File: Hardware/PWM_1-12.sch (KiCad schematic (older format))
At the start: 0 parts

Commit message: Renamed project
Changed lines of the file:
@@
 encoding utf-8
 Sheet 2 14
-Title ""
-Date ""
+Title "PWM 1-12"
+Date "2017-05-13"
 Rev ""
-Comp ""
-Comment1 ""
+Comp "WARG"
+Comment1 "Author: Stephen Cholvat"
 Comment2 ""
 Comment3 ""
@@
 	2700 950  2450 950
 Wire Wire Line
-	2450 550  2450 650
+	2450 650  2450 650
 Wire Wire Line
 	2450 650  2450 950
@@
 Wire Wire Line
 	7200 1750 8250 1750
-Text HLabel 1100 850  0    60   Input ~ 0
+Text HLabel 1100 950  0    60   Input ~ 0
 OC
-Text HLabel 1100 700  0    60   Input ~ 0
+Text HLabel 1100 800  0    60   Input ~ 0
 PWM
-Text HLabel 1100 1000 0    60   Input ~ 0
+Text HLabel 1100 1100 0    60   Input ~ 0
 SEL
-Text HLabel 1100 550  0    60   Input ~ 0
+Text HLabel 1100 650  0    60   Input ~ 0
 PWM_5V
 Wire Wire Line
-	2450 550  1100 550
+	2450 650  1100 650
 Connection ~ 2450 650
 Wire Bus Line
-	1100 700  1400 700
-Wire Bus Line
-	1100 850  1400 850
-Wire Bus Line
-	1100 1000 1400 1000
-Text Label 1200 700  0    60   ~ 0
+	1100 800  1400 800
+Wire Bus Line
+	1100 950  1400 950
+Wire Bus Line
+	1100 1100 1400 1100
+Text Label 1200 800  0    60   ~ 0
 PWM
-Text Label 1250 850  0    60   ~ 0
+Text Label 1250 950  0    60   ~ 0
 OC
-Text Label 1250 1000 0    60   ~ 0
+Text Label 1250 1100 0    60   ~ 0
 SEL
 $EndSCHEMATC

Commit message: ALL THE POWER
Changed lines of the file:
@@
 LIBS:valves
 LIBS:WARG
+LIBS:ZeroPilot-cache
 EELAYER 25 0
 EELAYER END
 $Descr A4 11693 8268
 encoding utf-8
-Sheet 2 14
+Sheet 2 15
 Title "PWM 1-12"
 Date "2017-05-13"
@@
 F4 "PWM" I L 2700 1250 60
 F5 "OC" I L 2700 1500 60
+F6 "SW_5V" I L 2700 1100 60
 $EndSheet
 $Sheet
@@
 F4 "PWM" I L 2700 2700 60
 F5 "OC" I L 2700 2950 60
+F6 "SW_5V" I L 2700 2550 60
 $EndSheet
 $Sheet
@@
 F4 "PWM" I L 2700 4200 60
 F5 "OC" I L 2700 4450 60
+F6 "SW_5V" I L 2700 4050 60
 $EndSheet
 $Sheet
@@
 F4 "PWM" I L 2700 5650 60
 F5 "OC" I L 2700 5900 60
+F6 "SW_5V" I L 2700 5500 60
 $EndSheet
 $Sheet
@@
 F4 "PWM" I L 5400 1250 60
 F5 "OC" I L 5400 1500 60
+F6 "SW_5V" I L 5400 1100 60
 $EndSheet
 $Sheet
@@
 F4 "PWM" I L 5400 2700 60
 F5 "OC" I L 5400 2950 60
+F6 "SW_5V" I L 5400 2550 60
 $EndSheet
 $Sheet
@@
 F4 "PWM" I L 5400 4200 60
 F5 "OC" I L 5400 4450 60
+F6 "SW_5V" I L 5400 4050 60
 $EndSheet
 $Sheet
@@
 F4 "PWM" I L 5400 5650 60
 F5 "OC" I L 5400 5900 60
+F6 "SW_5V" I L 5400 5500 60
 $EndSheet
 $Sheet
@@
 F4 "PWM" I L 8250 1250 60
 F5 "OC" I L 8250 1500 60
+F6 "SW_5V" I L 8250 1100 60
 $EndSheet
 $Sheet
@@
 F4 "PWM" I L 8250 2700 60
 F5 "OC" I L 8250 2950 60
+F6 "SW_5V" I L 8250 2550 60
 $EndSheet
 $Sheet
@@
 F4 "PWM" I L 8250 4200 60
 F5 "OC" I L 8250 4450 60
+F6 "SW_5V" I L 8250 4050 60
 $EndSheet
 $Sheet
@@
 F4 "PWM" I L 8250 5650 60
 F5 "OC" I L 8250 5900 60
+F6 "SW_5V" I L 8250 5500 60
 $EndSheet
 Entry Wire Line
@@
 SEL12
 Wire Wire Line
-	2700 950  2450 950
-Wire Wire Line
-	2450 650  2450 650
-Wire Wire Line
-	2450 650  2450 950
-Wire Wire Line
-	2450 950  2450 2400
-Wire Wire Line
-	2450 2400 2450 3900
-Wire Wire Line
-	2450 3900 2450 5350
-Wire Wire Line
-	2450 5350 2700 5350
-Wire Wire Line
-	5400 950  5400 2400
-Wire Wire Line
-	5400 2400 5400 3900
-Wire Wire Line
-	5400 3900 5400 5350
-Wire Wire Line
-	5400 950  5100 950
-Wire Wire Line
-	5100 650  5100 950
-Wire Wire Line
-	5100 950  5100 2400
-Wire Wire Line
-	5100 2400 5100 3900
-Wire Wire Line
-	5100 3900 5100 5350
-Wire Wire Line
-	5100 5350 5400 5350
-Wire Wire Line
-	5400 3900 5100 3900
-Connection ~ 5100 3900
-Connection ~ 5400 3900
-Wire Wire Line
-	5400 2400 5100 2400
-Connection ~ 5100 2400
-Connection ~ 5400 2400
-Wire Wire Line
-	8250 950  7950 950
-Wire Wire Line
-	7950 650  7950 950
-Wire Wire Line
-	7950 950  7950 2400
-Wire Wire Line
-	7950 2400 7950 3900
-Wire Wire Line
-	7950 3900 7950 5350
-Wire Wire Line
-	7950 5350 8250 5350
-Wire Wire Line
-	8250 3900 7950 3900
-Connection ~ 7950 3900
-Wire Wire Line
-	8250 2400 7950 2400
-Connection ~ 7950 2400
-Wire Wire Line
-	2450 650  5100 650
-Wire Wire Line
-	5100 650  7950 650
-Connection ~ 2450 950
-Connection ~ 7950 950
-Connection ~ 5100 650
-Connection ~ 5100 950
+	2700 950  2350 950
+Wire Wire Line
+	1100 650  1650 650
+Wire Wire Line
+	2350 5350 2700 5350
+Wire Wire Line
+	5400 950  5000 950
+Wire Wire Line
+	5000 5350 5400 5350
+Wire Wire Line
+	5400 3900 4950 3900
+Wire Wire Line
+	5400 2400 5000 2400
+Wire Wire Line
+	8250 950  7850 950
+Wire Wire Line
+	7850 5350 8250 5350
+Wire Wire Line
+	8250 3900 7800 3900
+Wire Wire Line
+	8250 2400 7850 2400
 Wire Bus Line
 	2150 900  2150 1150
@@
 	2250 5650 2700 5650
 Wire Wire Line
-	2700 3900 2450 3900
-Connection ~ 2450 3900
+	2700 3900 2350 3900
 Wire Wire Line
 	2250 4200 2700 4200
 Wire Wire Line
-	2700 2400 2450 2400
-Connection ~ 2450 2400
+	2700 2400 2350 2400
 Wire Wire Line
 	2700 2700 2250 2700
@@
 Wire Wire Line
 	7200 1750 8250 1750
+Text HLabel 1100 1100 0    60   Input ~ 0
+OC
 Text HLabel 1100 950  0    60   Input ~ 0
-OC
-Text HLabel 1100 800  0    60   Input ~ 0
 PWM
-Text HLabel 1100 1100 0    60   Input ~ 0
+Text HLabel 1100 1250 0    60   Input ~ 0
 SEL
 Text HLabel 1100 650  0    60   Input ~ 0
 PWM_5V
-Wire Wire Line
-	2450 650  1100 650
-Connection ~ 2450 650
-Wire Bus Line
-	1100 800  1400 800
 Wire Bus Line
 	1100 950  1400 950
 Wire Bus Line
 	1100 1100 1400 1100
-Text Label 1200 800  0    60   ~ 0
+Wire Bus Line
+	1100 1250 1400 1250
+Text Label 1200 950  0    60   ~ 0
 PWM
-Text Label 1250 950  0    60   ~ 0
+Text Label 1250 1100 0    60   ~ 0
 OC
-Text Label 1250 1100 0    60   ~ 0
+Text Label 1250 1250 0    60   ~ 0
 SEL
+Text Label 2350 950  0    60   ~ 0
+PWM_5V
+Text Label 2350 2400 0    60   ~ 0
+PWM_5V
+Text Label 2350 3900 0    60   ~ 0
+PWM_5V
+Text Label 2350 5350 0    60   ~ 0
+PWM_5V
+Text Label 5000 950  0    60   ~ 0
+PWM_5V
+Text Label 5000 2400 0    60   ~ 0
+PWM_5V
+Text Label 4950 3900 0    60   ~ 0
+PWM_5V
+Text Label 5000 5350 0    60   ~ 0
+PWM_5V
+Text Label 7850 950  0    60   ~ 0
+PWM_5V
+Text Label 7850 2400 0    60   ~ 0
+PWM_5V
+Text Label 7800 3900 0    60   ~ 0
+PWM_5V
+Text Label 7850 5350 0    60   ~ 0
+PWM_5V
+Text Label 1250 650  0    60   ~ 0
+PWM_5V
+Wire Wire Line
+	2700 1100 2350 1100
+Wire Wire Line
+	2350 2550 2700 2550
+Wire Wire Line
+	2350 4050 2700 4050
+Wire Wire Line
+	2700 5500 2350 5500
+Wire Wire Line
+	5000 5500 5400 5500
+Wire Wire Line
+	5000 4050 5400 4050
+Wire Wire Line
+	5000 2550 5400 2550
+Wire Wire Line
+	7850 5500 8250 5500
+Wire Wire Line
+	7850 4050 8250 4050
+Wire Wire Line
+	7850 2550 8250 2550
+Wire Wire Line
+	7850 1100 8250 1100
+Wire Wire Line
+	5000 1100 5400 1100
+Text Label 7850 1100 0    60   ~ 0
+SW_5V
+Text Label 7850 2550 0    60   ~ 0
+SW_5V
+Text Label 7850 4050 0    60   ~ 0
+SW_5V
+Text Label 5000 4050 0    60   ~ 0
+SW_5V
+Text Label 5000 2550 0    60   ~ 0
+SW_5V
+Text Label 5000 1100 0    60   ~ 0
+SW_5V
+Text Label 7850 5500 0    60   ~ 0
+SW_5V
+Text Label 5000 5500 0    60   ~ 0
+SW_5V
+Text Label 2350 5500 0    60   ~ 0
+SW_5V
+Text Label 2350 4050 0    60   ~ 0
+SW_5V
+Text Label 2350 2550 0    60   ~ 0
+SW_5V
+Text Label 2350 1100 0    60   ~ 0
+SW_5V
+Text HLabel 1100 800  0    60   Input ~ 0
+SW_5V
+Wire Wire Line
+	1100 800  1650 800
+Text Label 1250 800  0    60   ~ 0
+SW_5V
 $EndSCHEMATC

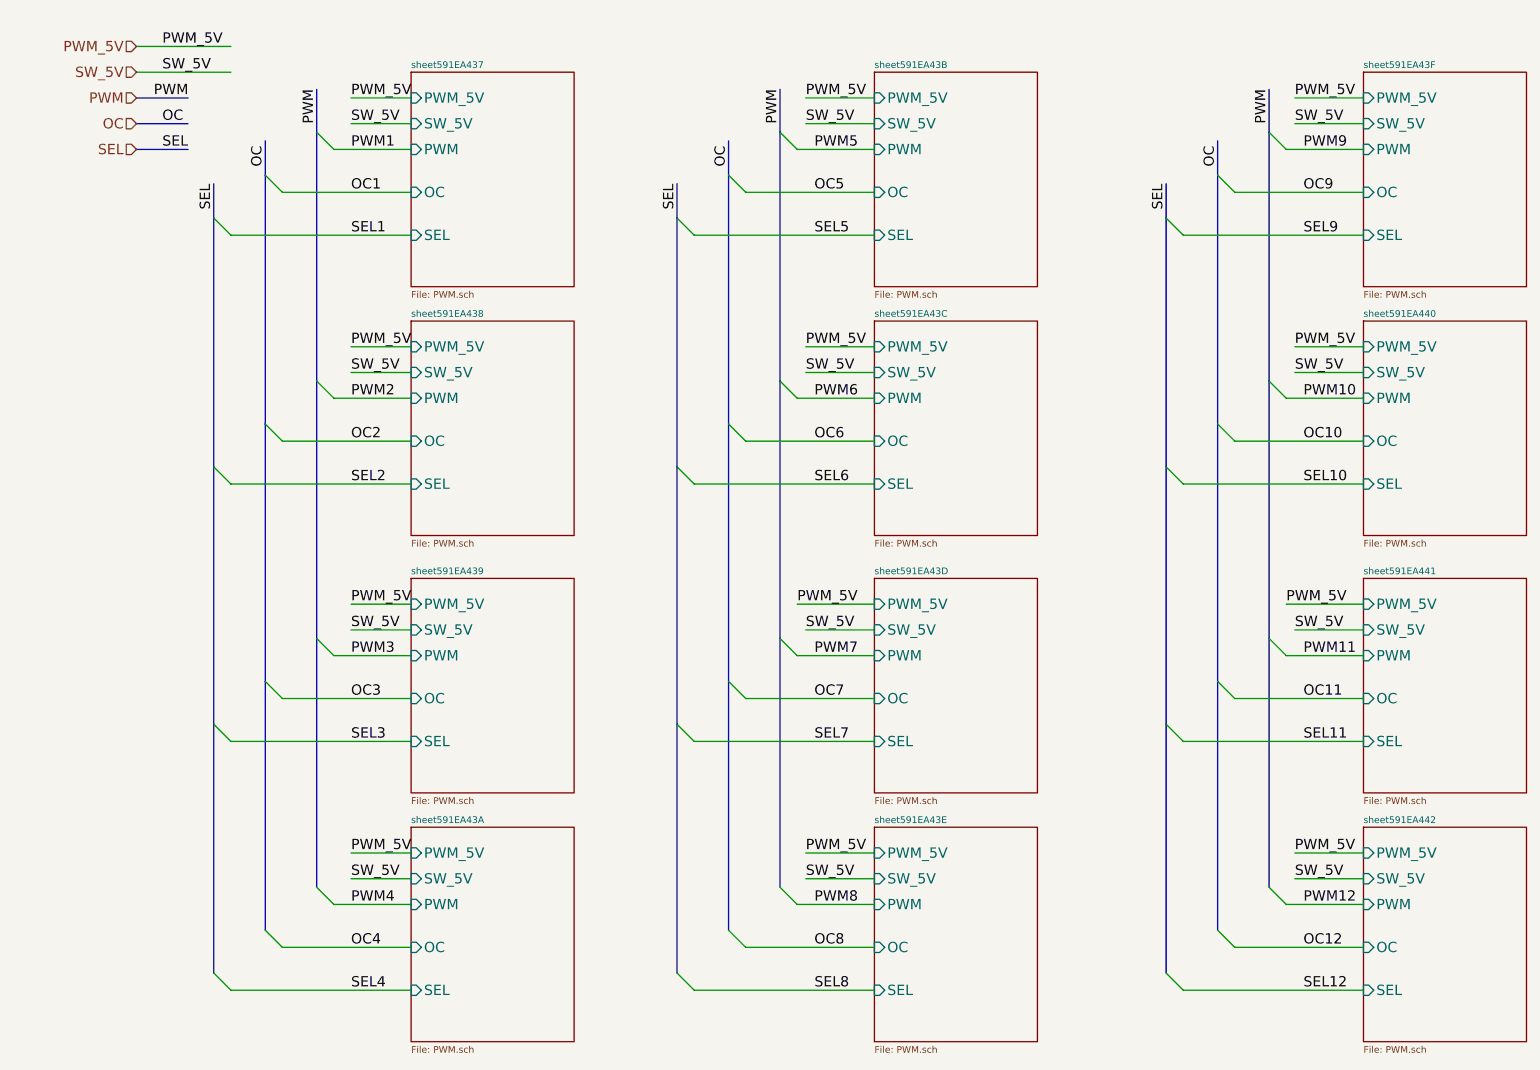
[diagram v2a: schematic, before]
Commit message: Added F7 chip
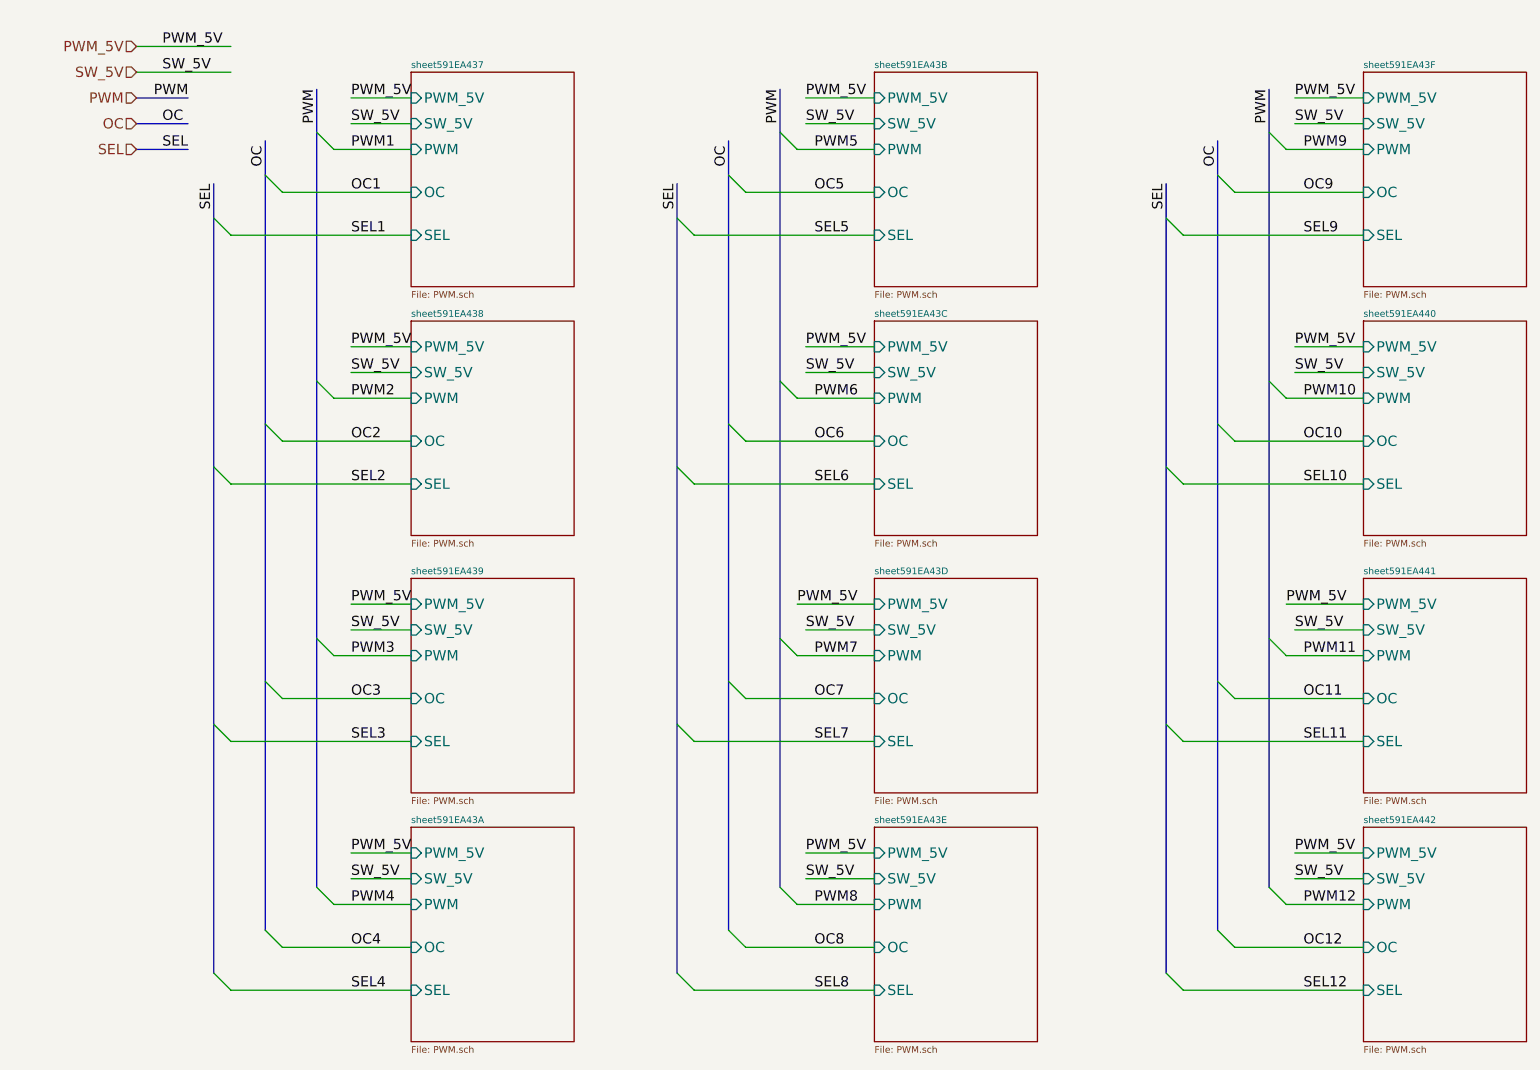
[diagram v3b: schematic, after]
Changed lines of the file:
@@
 EESchema Schematic File Version 2
+LIBS:WARG
 LIBS:power
 LIBS:device
@@
 LIBS:contrib
 LIBS:valves
-LIBS:WARG
-LIBS:ZeroPilot-cache
 EELAYER 25 0
 EELAYER END
 $Descr A4 11693 8268
 encoding utf-8
-Sheet 2 15
+Sheet 2 17
 Title "PWM 1-12"
 Date "2017-05-13"
@@
 	8250 2400 7850 2400
 Wire Bus Line
-	2150 900  2150 1150
-Wire Bus Line
-	2150 1150 2150 2600
-Wire Bus Line
-	2150 2600 2150 4100
-Wire Bus Line
-	2150 4100 2150 5550
+	2150 900  2150 5550
 Wire Wire Line
 	2250 5650 2700 5650
@@
 	2250 1250 2700 1250
 Wire Bus Line
-	1850 1200 1850 1400
-Wire Bus Line
-	1850 1400 1850 2850
-Wire Bus Line
-	1850 2850 1850 4350
-Wire Bus Line
-	1850 4350 1850 5800
+	1850 1200 1850 5800
 Wire Wire Line
 	1950 5900 2700 5900
@@
 	1950 1500 2700 1500
 Wire Bus Line
-	1550 1450 1550 1650
-Wire Bus Line
-	1550 1650 1550 3100
-Wire Bus Line
-	1550 3100 1550 4600
-Wire Bus Line
-	1550 4600 1550 6050
+	1550 1450 1550 6050
 Wire Wire Line
 	1650 6150 2700 6150
@@
 	1650 1750 2700 1750
 Wire Bus Line
-	4850 900  4850 1150
-Wire Bus Line
-	4850 1150 4850 2600
-Wire Bus Line
-	4850 2600 4850 4100
-Wire Bus Line
-	4850 4100 4850 5550
+	4850 900  4850 5550
 Wire Wire Line
 	4950 5650 5400 5650
@@
 	4950 1250 5400 1250
 Wire Bus Line
-	4550 1200 4550 1400
-Wire Bus Line
-	4550 1400 4550 2850
-Wire Bus Line
-	4550 2850 4550 4350
-Wire Bus Line
-	4550 4350 4550 5800
+	4550 1200 4550 5800
 Wire Wire Line
 	4650 5900 5400 5900
@@
 	4650 1500 5400 1500
 Wire Bus Line
-	4250 1450 4250 1650
-Wire Bus Line
-	4250 1650 4250 3100
-Wire Bus Line
-	4250 3100 4250 4600
-Wire Bus Line
-	4250 4600 4250 6050
+	4250 1450 4250 6050
 Wire Wire Line
 	4350 6150 5400 6150
@@
 	4350 1750 5400 1750
 Wire Bus Line
-	7700 900  7700 1150
-Wire Bus Line
-	7700 1150 7700 2600
-Wire Bus Line
-	7700 2600 7700 4100
-Wire Bus Line
-	7700 4100 7700 5550
+	7700 900  7700 5550
 Wire Wire Line
 	7800 5650 8250 5650
@@
 	7800 1250 8250 1250
 Wire Bus Line
-	7400 1200 7400 1400
-Wire Bus Line
-	7400 1400 7400 2850
-Wire Bus Line
-	7400 2850 7400 4350
-Wire Bus Line
-	7400 4350 7400 5800
+	7400 1200 7400 5800
 Wire Wire Line
 	7500 5900 8250 5900
@@
 	7500 1500 8250 1500
 Wire Bus Line
-	7100 1450 7100 1650
-Wire Bus Line
-	7100 1650 7100 3100
-Wire Bus Line
-	7100 3100 7100 4600
-Wire Bus Line
-	7100 4600 7100 6050
+	7100 1450 7100 6050
 Wire Wire Line
 	7200 6150 8250 6150

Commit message: Added F7 Circuitry
Added way too much for 1 commit.
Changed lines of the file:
@@
 LIBS:contrib
 LIBS:valves
+LIBS:ZeroPilot-cache
 EELAYER 25 0
 EELAYER END
 $Descr A4 11693 8268
 encoding utf-8
-Sheet 2 18
+Sheet 2 17
 Title "PWM 1-12"
 Date "2017-05-13"
@@
 PWM4
 Text Label 2150 1100 1    60   ~ 0
-PWM
+PWM[1..12]
 Entry Wire Line
 	1850 5800 1950 5900
@@
 	1850 1400 1950 1500
 Text Label 1850 1350 1    60   ~ 0
-OC
+OC[1..12]
 Entry Wire Line
 	1550 6050 1650 6150
@@
 	1550 1650 1650 1750
 Text Label 1550 1600 1    60   ~ 0
-SEL
+SEL[1..12]
 Text Label 2350 1500 0    60   ~ 0
 OC1
@@
 PWM8
 Text Label 4850 1100 1    60   ~ 0
-PWM
+PWM[1..12]
 Entry Wire Line
 	4550 5800 4650 5900
@@
 	4550 1400 4650 1500
 Text Label 4550 1350 1    60   ~ 0
-OC
+OC[1..12]
 Entry Wire Line
 	4250 6050 4350 6150
@@
 	4250 1650 4350 1750
 Text Label 4250 1600 1    60   ~ 0
-SEL
+SEL[1..12]
 Text Label 5050 1500 0    60   ~ 0
 OC5
@@
 PWM12
 Text Label 7700 1100 1    60   ~ 0
-PWM
+PWM[1..12]
 Entry Wire Line
 	7400 5800 7500 5900
@@
 	7400 1400 7500 1500
 Text Label 7400 1350 1    60   ~ 0
-OC
+OC[1..12]
 Entry Wire Line
 	7100 6050 7200 6150
@@
 	7100 1650 7200 1750
 Text Label 7100 1600 1    60   ~ 0
-SEL
+SEL[1..12]
 Text Label 7900 1500 0    60   ~ 0
 OC9
@@
 Text Label 7900 6150 0    60   ~ 0
 SEL12
-Wire Wire Line
-	2700 950  2350 950
-Wire Wire Line
-	1100 650  1650 650
-Wire Wire Line
-	2350 5350 2700 5350
-Wire Wire Line
-	5400 950  5000 950
-Wire Wire Line
-	5000 5350 5400 5350
-Wire Wire Line
-	5400 3900 4950 3900
-Wire Wire Line
-	5400 2400 5000 2400
-Wire Wire Line
-	8250 950  7850 950
-Wire Wire Line
-	7850 5350 8250 5350
-Wire Wire Line
-	8250 3900 7800 3900
-Wire Wire Line
-	8250 2400 7850 2400
 Wire Bus Line
 	2150 900  2150 5550
@@
 	2250 5650 2700 5650
 Wire Wire Line
-	2700 3900 2350 3900
-Wire Wire Line
 	2250 4200 2700 4200
-Wire Wire Line
-	2700 2400 2350 2400
 Wire Wire Line
 	2700 2700 2250 2700
@@
 	7200 1750 8250 1750
 Text HLabel 1100 1100 0    60   Input ~ 0
-OC
+OC[1..12]
 Text HLabel 1100 950  0    60   Input ~ 0
-PWM
+PWM[1..12]
 Text HLabel 1100 1250 0    60   Input ~ 0
-SEL
+SEL[1..12]
 Text HLabel 1100 650  0    60   Input ~ 0
 PWM_5V
@@
 	1100 1250 1400 1250
 Text Label 1200 950  0    60   ~ 0
-PWM
-Text Label 1250 1100 0    60   ~ 0
-OC
+PWM[1..12]
+Text Label 1150 1100 0    60   ~ 0
+OC[1..12]
 Text Label 1250 1250 0    60   ~ 0
-SEL
-Text Label 2350 950  0    60   ~ 0
-PWM_5V
-Text Label 2350 2400 0    60   ~ 0
-PWM_5V
-Text Label 2350 3900 0    60   ~ 0
-PWM_5V
-Text Label 2350 5350 0    60   ~ 0
-PWM_5V
-Text Label 5000 950  0    60   ~ 0
-PWM_5V
-Text Label 5000 2400 0    60   ~ 0
-PWM_5V
-Text Label 4950 3900 0    60   ~ 0
-PWM_5V
-Text Label 5000 5350 0    60   ~ 0
-PWM_5V
-Text Label 7850 950  0    60   ~ 0
-PWM_5V
-Text Label 7850 2400 0    60   ~ 0
-PWM_5V
-Text Label 7800 3900 0    60   ~ 0
-PWM_5V
-Text Label 7850 5350 0    60   ~ 0
-PWM_5V
-Text Label 1250 650  0    60   ~ 0
-PWM_5V
-Wire Wire Line
-	2700 1100 2350 1100
-Wire Wire Line
-	2350 2550 2700 2550
-Wire Wire Line
-	2350 4050 2700 4050
-Wire Wire Line
-	2700 5500 2350 5500
-Wire Wire Line
-	5000 5500 5400 5500
-Wire Wire Line
-	5000 4050 5400 4050
-Wire Wire Line
-	5000 2550 5400 2550
-Wire Wire Line
-	7850 5500 8250 5500
-Wire Wire Line
-	7850 4050 8250 4050
-Wire Wire Line
-	7850 2550 8250 2550
-Wire Wire Line
-	7850 1100 8250 1100
-Wire Wire Line
-	5000 1100 5400 1100
-Text Label 7850 1100 0    60   ~ 0
-SW_5V
-Text Label 7850 2550 0    60   ~ 0
-SW_5V
-Text Label 7850 4050 0    60   ~ 0
-SW_5V
-Text Label 5000 4050 0    60   ~ 0
-SW_5V
-Text Label 5000 2550 0    60   ~ 0
-SW_5V
-Text Label 5000 1100 0    60   ~ 0
-SW_5V
-Text Label 7850 5500 0    60   ~ 0
-SW_5V
-Text Label 5000 5500 0    60   ~ 0
-SW_5V
-Text Label 2350 5500 0    60   ~ 0
-SW_5V
-Text Label 2350 4050 0    60   ~ 0
-SW_5V
-Text Label 2350 2550 0    60   ~ 0
-SW_5V
-Text Label 2350 1100 0    60   ~ 0
+SEL[1..12]
+Text Label 2700 950  2    60   ~ 0
+PWM_5V
+Text Label 2700 2400 2    60   ~ 0
+PWM_5V
+Text Label 2700 3900 2    60   ~ 0
+PWM_5V
+Text Label 2700 5350 2    60   ~ 0
+PWM_5V
+Text Label 5400 950  2    60   ~ 0
+PWM_5V
+Text Label 5400 2400 2    60   ~ 0
+PWM_5V
+Text Label 5400 3900 2    60   ~ 0
+PWM_5V
+Text Label 5400 5350 2    60   ~ 0
+PWM_5V
+Text Label 8250 950  2    60   ~ 0
+PWM_5V
+Text Label 8250 2400 2    60   ~ 0
+PWM_5V
+Text Label 8250 3900 2    60   ~ 0
+PWM_5V
+Text Label 8250 5350 2    60   ~ 0
+PWM_5V
+Text Label 1100 650  0    60   ~ 0
+PWM_5V
+Text Label 8250 1100 2    60   ~ 0
+SW_5V
+Text Label 8250 2550 2    60   ~ 0
+SW_5V
+Text Label 8250 4050 2    60   ~ 0
+SW_5V
+Text Label 5400 4050 2    60   ~ 0
+SW_5V
+Text Label 5400 2550 2    60   ~ 0
+SW_5V
+Text Label 5400 1100 2    60   ~ 0
+SW_5V
+Text Label 8250 5500 2    60   ~ 0
+SW_5V
+Text Label 5400 5500 2    60   ~ 0
+SW_5V
+Text Label 2700 5500 2    60   ~ 0
+SW_5V
+Text Label 2700 4050 2    60   ~ 0
+SW_5V
+Text Label 2700 2550 2    60   ~ 0
+SW_5V
+Text Label 2700 1100 2    60   ~ 0
 SW_5V
 Text HLabel 1100 800  0    60   Input ~ 0
 SW_5V
-Wire Wire Line
-	1100 800  1650 800
-Text Label 1250 800  0    60   ~ 0
+Text Label 1100 800  0    60   ~ 0
 SW_5V
 $EndSCHEMATC
